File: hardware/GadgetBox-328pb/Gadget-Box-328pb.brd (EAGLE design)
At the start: 93.5 x 53.5 mm, 36 parts, among them IC1A ATMEGA328PB-AU, IC1B ATMEGA328PB-MU, U1 MCP73831T-2ACI/OT, U2 AP2112-3.3, X1 CRYSTAL-0500290P1

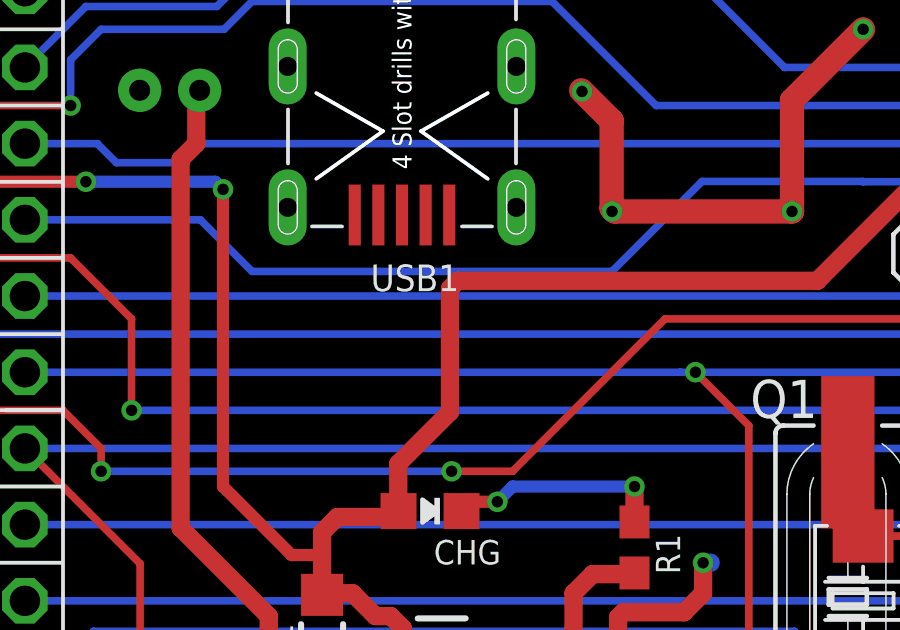
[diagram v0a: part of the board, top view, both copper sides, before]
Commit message: Connect VCC from USB connector to 5V0. Ooops!
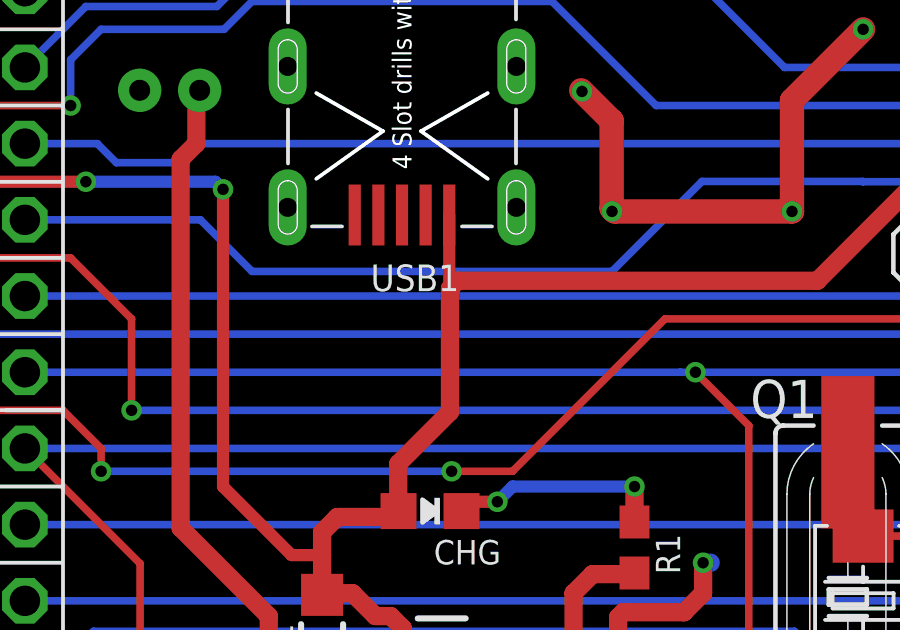
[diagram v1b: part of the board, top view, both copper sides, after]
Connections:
- removed net VBUS: USB1.1
- net 5V0: now also USB1.1
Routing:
- net 5V0: track 222.3 -> 225.0 mm
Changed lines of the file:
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@@
 <wire x1="23.622" y1="28.194" x2="23.622" y2="26.908" width="0.4064" layer="1"/>
 <wire x1="23.622" y1="26.908" x2="23.693" y2="26.837" width="0.4064" layer="1"/>
-<wire x1="25.6" y1="43.434" x2="25.6" y2="39.316" width="0.6096" layer="1"/>
+<wire x1="25.6" y1="43.434" x2="25.6" y2="43.18" width="0.6096" layer="1"/>
+<wire x1="25.6" y1="43.18" x2="25.6" y2="39.316" width="0.6096" layer="1"/>
 <wire x1="25.6" y1="39.316" x2="23.876" y2="37.592" width="0.6096" layer="1"/>
 <wire x1="23.876" y1="37.592" x2="23.876" y2="36.021" width="0.6096" layer="1"/>
@@
 <wire x1="13.462" y1="46.99" x2="17.78" y2="46.99" width="0.4064" layer="16"/>
 <wire x1="17.78" y1="46.99" x2="18.034" y2="46.736" width="0.4064" layer="16"/>
+<contactref element="USB1" pad="1"/>
+<wire x1="25.5748" y1="45.881" x2="25.5748" y2="43.2052" width="0.4064" layer="1"/>
+<wire x1="25.5748" y1="43.2052" x2="25.6" y2="43.18" width="0.4064" layer="1"/>
 </signal>
 <signal name="VBAT">
@@
 <wire x1="49.27" y1="47.2" x2="49.276" y2="47.206" width="0.254" layer="1"/>
 </signal>
-<signal name="VBUS">
-<contactref element="USB1" pad="1"/>
-</signal>
 </signals>

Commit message: wip
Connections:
- net 5V0: no longer AH.5V@2, AL.5V@2, BH.5V@2, BL.5V@2
- net RESET: no longer AH.RESET@2, AL.RESET@2, BH.RESET@2, BL.RESET@2
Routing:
- net RESET: track 185.4 -> 119.2 mm, vias 4 -> 2
- net 5V0: track 225.0 -> 185.8 mm
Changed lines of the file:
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@@
 </signal>
 <signal name="RESET">
-<contactref element="AL" pad="RESET@2"/>
-<contactref element="AH" pad="RESET@2"/>
-<contactref element="BL" pad="RESET@2"/>
-<contactref element="BH" pad="RESET@2"/>
 <contactref element="IC1A" pad="29"/>
 <contactref element="IC1B" pad="29"/>
@@
 <wire x1="88.9" y1="49.53" x2="90.17" y2="48.26" width="0.254" layer="16"/>
 <wire x1="90.17" y1="48.26" x2="90.17" y2="46.482" width="0.254" layer="16"/>
-<wire x1="90.17" y1="46.482" x2="93.472" y2="43.18" width="0.254" layer="16"/>
 <wire x1="50.75848125" y1="31.25816875" x2="50.81616875" y2="31.25816875" width="0.254" layer="1"/>
 <wire x1="50.81616875" y1="31.25816875" x2="53.213" y2="33.655" width="0.254" layer="1"/>
@@
 <wire x1="50.2158" y1="30.7154875" x2="50.75848125" y2="31.25816875" width="0.2032" layer="1"/>
 <via x="12.954" y="49.53" extent="1-16" drill="0.381"/>
-<wire x1="4.826" y1="42.926" x2="2.54" y2="40.64" width="0.254" layer="1"/>
-<wire x1="93.472" y1="43.18" x2="93.218" y2="43.18" width="0.254" layer="16"/>
-<wire x1="93.218" y1="43.18" x2="91.948" y2="41.91" width="0.254" layer="16"/>
-<wire x1="91.948" y1="41.91" x2="91.948" y2="31.496" width="0.254" layer="16"/>
-<via x="91.948" y="31.496" extent="1-16" drill="0.381"/>
-<wire x1="91.948" y1="31.496" x2="91.948" y2="22.352" width="0.254" layer="1"/>
-<via x="91.948" y="22.352" extent="1-16" drill="0.381"/>
-<wire x1="91.948" y1="22.352" x2="91.948" y2="16.764" width="0.254" layer="16"/>
-<wire x1="91.948" y1="16.764" x2="93.472" y2="15.24" width="0.254" layer="16"/>
-<wire x1="2.54" y1="40.64" x2="2.54" y2="17.272" width="0.254" layer="1"/>
-<wire x1="2.54" y1="17.272" x2="3.81" y2="16.002" width="0.254" layer="1"/>
-<wire x1="3.81" y1="16.002" x2="3.81" y2="13.97" width="0.254" layer="1"/>
-<wire x1="3.81" y1="13.97" x2="2.54" y2="12.7" width="0.254" layer="1"/>
 <wire x1="12.954" y1="49.53" x2="7.62" y2="49.53" width="0.254" layer="1"/>
 <wire x1="7.62" y1="49.53" x2="4.826" y2="46.736" width="0.254" layer="1"/>
@@
 <contactref element="CHG" pad="A"/>
 <contactref element="PSW1" pad="1"/>
-<contactref element="BH" pad="5V@2"/>
-<contactref element="AL" pad="5V@2"/>
-<contactref element="AH" pad="5V@2"/>
-<contactref element="BL" pad="5V@2"/>
 <wire x1="24.0237" y1="31.7348" x2="24.0237" y2="32.1103" width="0.6096" layer="1"/>
 <wire x1="24.0237" y1="32.1103" x2="23.622" y2="32.512" width="0.6096" layer="1"/>
@@
 <wire x1="37.846" y1="43.688" x2="25.854" y2="43.688" width="0.6096" layer="1"/>
 <wire x1="25.854" y1="43.688" x2="25.6" y2="43.434" width="0.6096" layer="1"/>
-<wire x1="93.472" y1="12.7" x2="91.694" y2="12.7" width="0.6096" layer="1"/>
-<wire x1="91.694" y1="12.7" x2="90.424" y2="13.97" width="0.6096" layer="1"/>
-<wire x1="90.424" y1="13.97" x2="90.424" y2="16.764" width="0.6096" layer="1"/>
-<wire x1="90.424" y1="16.764" x2="93.472" y2="19.812" width="0.6096" layer="1"/>
-<wire x1="93.472" y1="19.812" x2="93.472" y2="40.64" width="0.6096" layer="1"/>
 <wire x1="65.532" y1="53.848" x2="72.152" y2="53.848" width="0.6096" layer="1"/>
 <wire x1="72.152" y1="53.848" x2="74" y2="52" width="0.6096" layer="1"/>
-<wire x1="93.472" y1="40.64" x2="92.964" y2="40.64" width="0.4064" layer="1"/>
 <wire x1="92.964" y1="40.64" x2="92.202" y2="41.402" width="0.4064" layer="1"/>
 <wire x1="92.202" y1="41.402" x2="92.202" y2="42.926" width="0.4064" layer="1"/>
@@
 <wire x1="47.498" y1="53.34" x2="65.024" y2="53.34" width="0.6096" layer="1"/>
 <wire x1="65.024" y1="53.34" x2="65.532" y2="53.848" width="0.6096" layer="1"/>
-<wire x1="2.54" y1="15.24" x2="4.318" y2="15.24" width="0.4064" layer="16"/>
 <wire x1="4.318" y1="15.24" x2="8.128" y2="11.43" width="0.4064" layer="16"/>
 <wire x1="25.146" y1="12.192" x2="25.146" y2="23.114" width="0.4064" layer="1"/>
@@
 <wire x1="18.034" y1="36.83" x2="20.32" y2="34.544" width="0.4064" layer="1"/>
 <wire x1="20.32" y1="34.544" x2="21.336" y2="34.544" width="0.4064" layer="1"/>
-<wire x1="2.54" y1="43.18" x2="6.35" y2="46.99" width="0.4064" layer="16"/>
 <via x="18.034" y="46.736" extent="1-16" drill="0.381"/>
 <wire x1="6.35" y1="46.99" x2="7.874" y2="46.99" width="0.4064" layer="16"/>

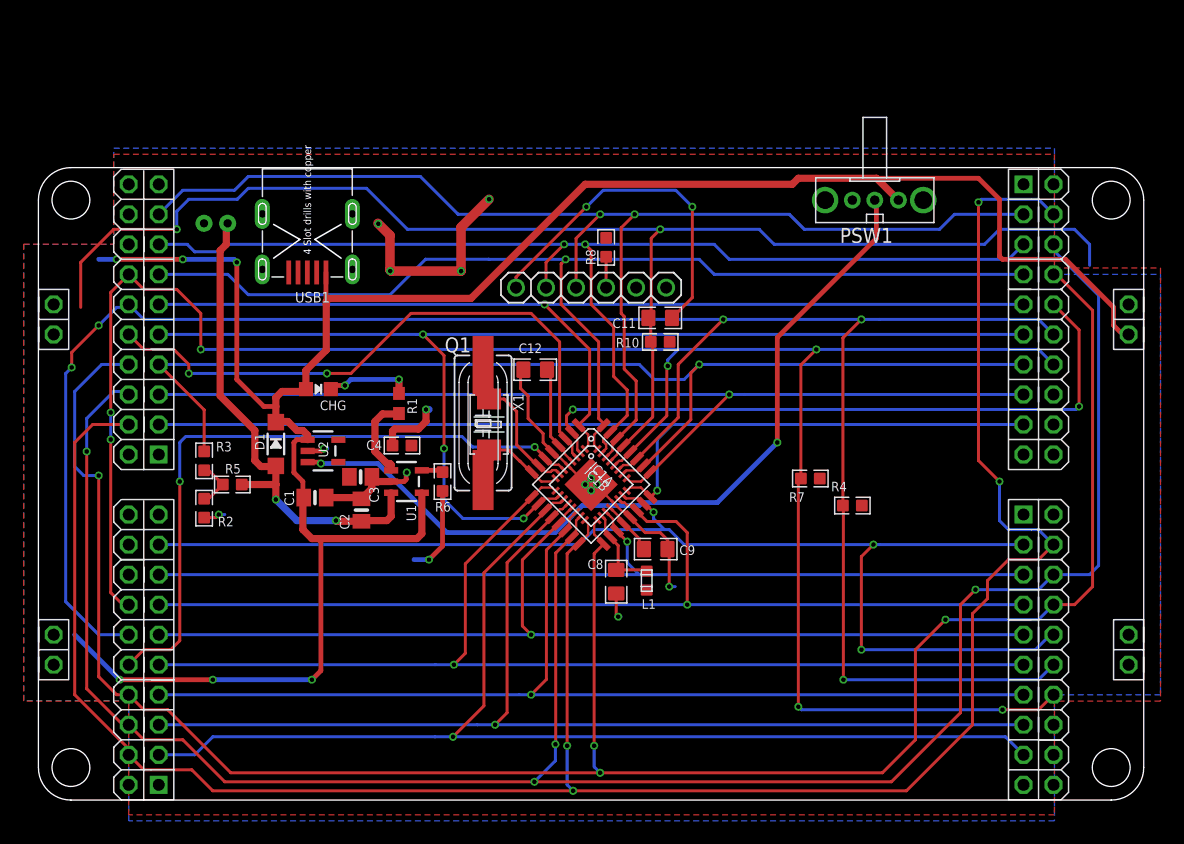
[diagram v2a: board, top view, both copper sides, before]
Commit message: updated eCog connectors to newer version footprint
finor rerouting and other minor repair of an airwire
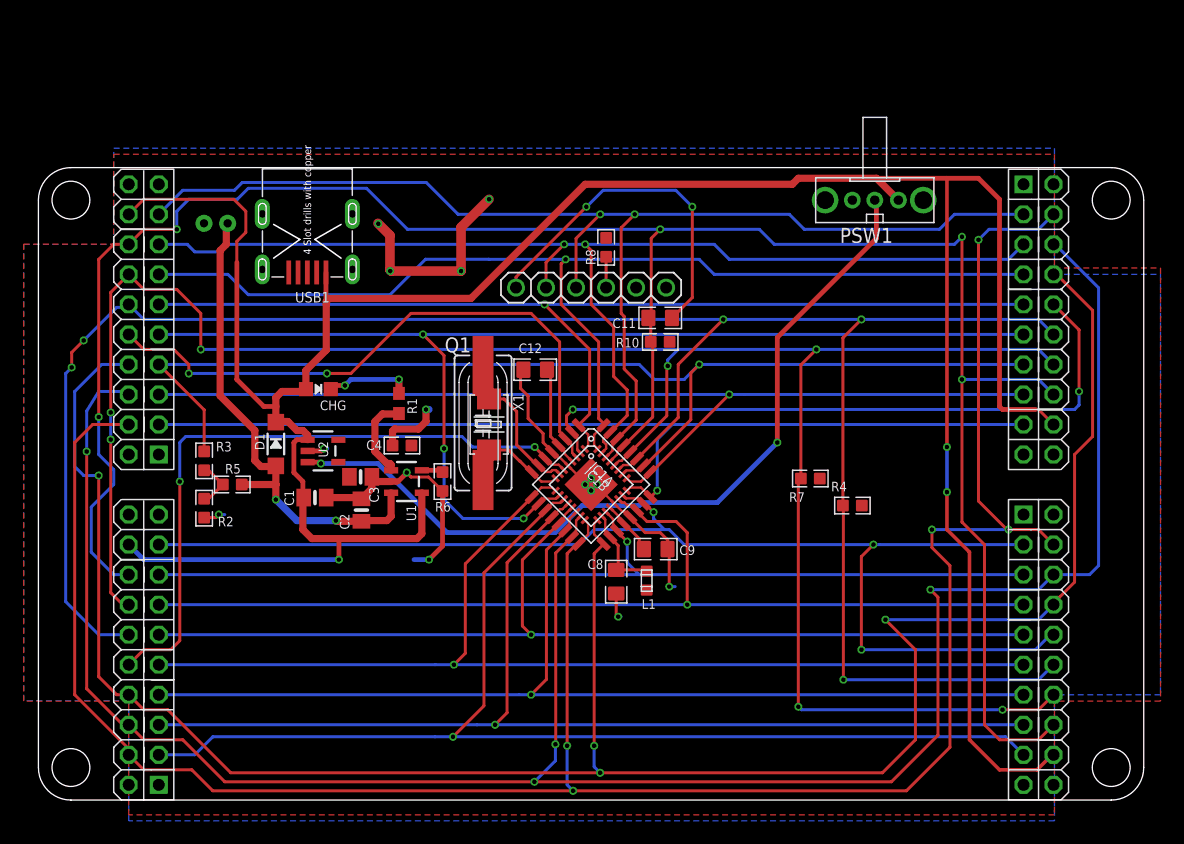
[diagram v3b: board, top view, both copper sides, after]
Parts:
- AH, AL, BH, BL: value ECOGECOG_SLOT_ALT1 -> ECOGECOG_SLOT; device eCogs:ECOG_ALT1 -> eCogs:ECOG
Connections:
- net 5V0: now also AH.5V@B7, AL.5V@B7, BH.5V@B7, BL.5V@B7
- net RESET: now also AH.RESET@B6, AL.RESET@B6, BH.RESET@B6, BL.RESET@B6
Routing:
- net RESET: track 119.2 -> 187.7 mm, vias 2 -> 5
- net 5V0: track 185.8 -> 236.5 mm, vias 6 -> 3
- net SPI-SCK: track 180.0 -> 184.0 mm
- net SPI-MOSI: track 182.2 -> 185.8 mm
- net GND: track 70.3 -> 73.7 mm
- net SPI-MISO: track 192.1 -> 192.6 mm, vias 4 -> 5

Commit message: GadgetBox 328pb Version 1.3
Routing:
- net D0/RX/MISO: track 106.1 -> 107.6 mm
- net RESET: track 187.7 -> 188.5 mm
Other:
- board text added: "+ -"
- board text added: "<-Cutout"
- board text added: "Gadget Box - ATmega328PB Copyright 2016 Gadget Factory, LLC Version 1.3"
- board text removed: "Gadget Box - ATmega328PB Copyright 2016 Gadget Factory, LLC Version 1.2"
